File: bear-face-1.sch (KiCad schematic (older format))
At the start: 177 parts, among them J1 Conn_01x04, SW1 SW_Push, U1 Elite-C

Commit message: Diodes, silkscreen updated
Changed diodes back to THT diodes to avoid track issues. Intend to use 1N4148 diodes
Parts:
- added H8: Hole, MountingHole:MountingHole_2.1mm, symbol keebio:Hole
- D1, D10, D11, D12, D13, D14, D15, D16, D17, D18, D19, D2, D20, D21, D22, D23, D24, D25, D26, D27, D28, D29, D3, D30, D31, D32, D33, D34, D35, D36, D37, D38, D39, D4, D40, D41, D42, D43, D44, D45, D46, D47, D48, D49, D5, D50, D51, D52, D53, D54, D55, D56, D57, D58, D59, D6, D60, D61, D62, D63, D64, D65, D66, D67, D68, D69, D7, D70, D71, D72, D73, D74, D75, D76, D77, D78, D79, D8, D80, D81, D82, D83, D9: footprint Keebio-Parts:Diode-dual -> Keebio-Parts:Diode

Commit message: Added hole for plate ground
Stock plate has a hole grounding the plate to the PCB. Added this hole as a 3mm mounting hole (H8)
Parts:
- H8: footprint MountingHole:MountingHole_2.1mm -> MountingHole:MountingHole_3mm
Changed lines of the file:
@@
 F 0 "H8" H 3186 2053 60  0000 L CNN
 F 1 "Hole" H 3186 1947 60  0000 L CNN
-F 2 "MountingHole:MountingHole_2.1mm" H 3000 2000 60  0001 C CNN
+F 2 "MountingHole:MountingHole_3mm" H 3000 2000 60  0001 C CNN
 F 3 "" H 3000 2000 60  0001 C CNN
 	1    3000 2000

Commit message: Matrix, footprints changed
Changed to pure rectangular matrix, updated switch and diode SilkS, anticipate using on-board 32u4
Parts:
- removed J1: Conn_01x04, Connector_Wire:SolderWirePad_1x04_P3.175mm_Drill0.8mm, symbol Connector_Generic:Conn_01x04
- removed U1: Elite-C, Keebio-Parts:Elite-C, symbol keebio:Elite-C
- added F1: 500mA, Fuse:Fuse_1206_3216Metric, symbol Device:Polyfuse_Small
- renumbered D11 to D1, D16 to D10, D17 to D11, D7 to D12, D8 to D13, D18 to D14, D10 to D15, D21 to D16, D22 to D17, D12 to D18, D23 to D19, D1 to D2, D14 to D20, D24 to D21, D33 to D22, D34 to D23, D25 to D24, D35 to D25, D36 to D28, D28 to D29, D2 to D3, D20 to D30, D30 to D31, D31 to D32, D40 to D33, D32 to D34, D41 to D35, D51 to D36, D42 to D37, D43 to D38, D52 to D39, D13 to D4, D44 to D40, D53 to D41, D45 to D42, D46 to D43, D37 to D44, D9 to D45, D39 to D46, D58 to D47, D49 to D48, D59 to D49, D3 to D5, D60 to D51, D70 to D52, D61 to D53, D71 to D54, D62 to D55, D63 to D56, D54 to D57, D55 to D58, D19 to D59, D4 to D6, D48 to D60, D67 to D61, D76 to D62, D68 to D63, D77 to D64, D69 to D65, D79 to D66, D80 to D67, D81 to D68, D72 to D69, D5 to D7, D73 to D70, D64 to D71, D29 to D72, D38 to D73, D57 to D74, D66 to D75, D75 to D76, D78 to D77, D82 to D78, D83 to D79, D15 to D8, D74 to D80, D65 to D81, D56 to D82, D47 to D83, D6 to D9, H3 to H2, H5 to H3, H7 to H4, H2 to H5, H4 to H6, H6 to H7, MX11 to MX1, MX16 to MX10, MX17 to MX11, MX7 to MX12, MX8 to MX13, MX18 to MX14, MX10 to MX15, MX21 to MX16, MX22 to MX17, MX12 to MX18, MX23 to MX19, MX1 to MX2, MX14 to MX20, MX24 to MX21, MX33 to MX22, MX34 to MX23, MX25 to MX24, MX35 to MX25, MX36 to MX28, MX28 to MX29, MX2 to MX3, MX20 to MX30, MX30 to MX31, MX31 to MX32, MX40 to MX33, MX32 to MX34, MX41 to MX35, MX51 to MX36, MX42 to MX37, MX43 to MX38, MX52 to MX39, MX13 to MX4, MX44 to MX40, MX53 to MX41, MX45 to MX42, MX46 to MX43, MX37 to MX44, MX9 to MX45, MX39 to MX46, MX58 to MX47, MX49 to MX48, MX59 to MX49, MX3 to MX5, MX60 to MX51, MX70 to MX52, MX61 to MX53, MX71 to MX54, MX62 to MX55, MX63 to MX56, MX54 to MX57, MX55 to MX58, MX19 to MX59, MX4 to MX6, MX48 to MX60, MX67 to MX61, MX76 to MX62, MX68 to MX63, MX77 to MX64, MX69 to MX65, MX79 to MX66, MX80 to MX67, MX81 to MX68, MX72 to MX69, MX5 to MX7, MX73 to MX70, MX64 to MX71, MX29 to MX72, MX38 to MX73, MX57 to MX74, MX66 to MX75, MX75 to MX76, MX78 to MX77, MX82 to MX78, MX83 to MX79, MX15 to MX8, MX74 to MX80, MX65 to MX81, MX56 to MX82, MX47 to MX83, MX6 to MX9
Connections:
- net labels added: COL10, COL11, COL12, COL13, COL14
- net labels removed: ROW6, ROW7, ROW8
- wire segments 260 -> 254
- no-connect marks 5 -> 0
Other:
- moved on the sheet: D1, D10, D11, D12, D13, D14, D15, D16, D17, D18, D19, D2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

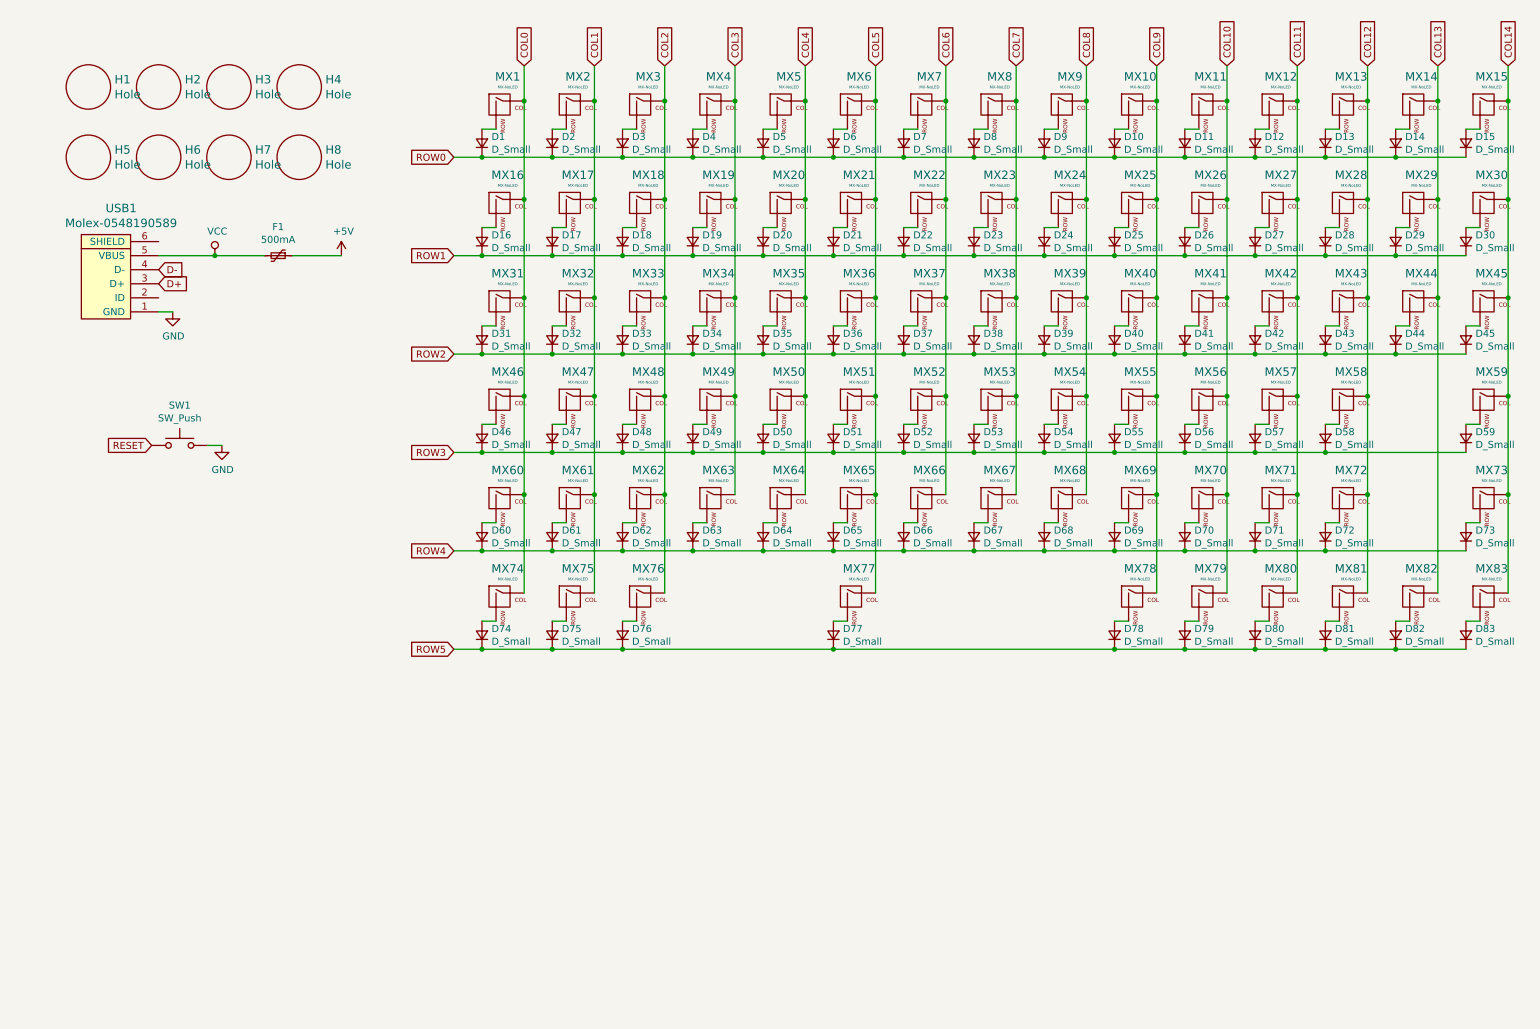
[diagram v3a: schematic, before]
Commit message: MCU added, diodes changed
Changed to SMD components, matched components used in ai03's guide
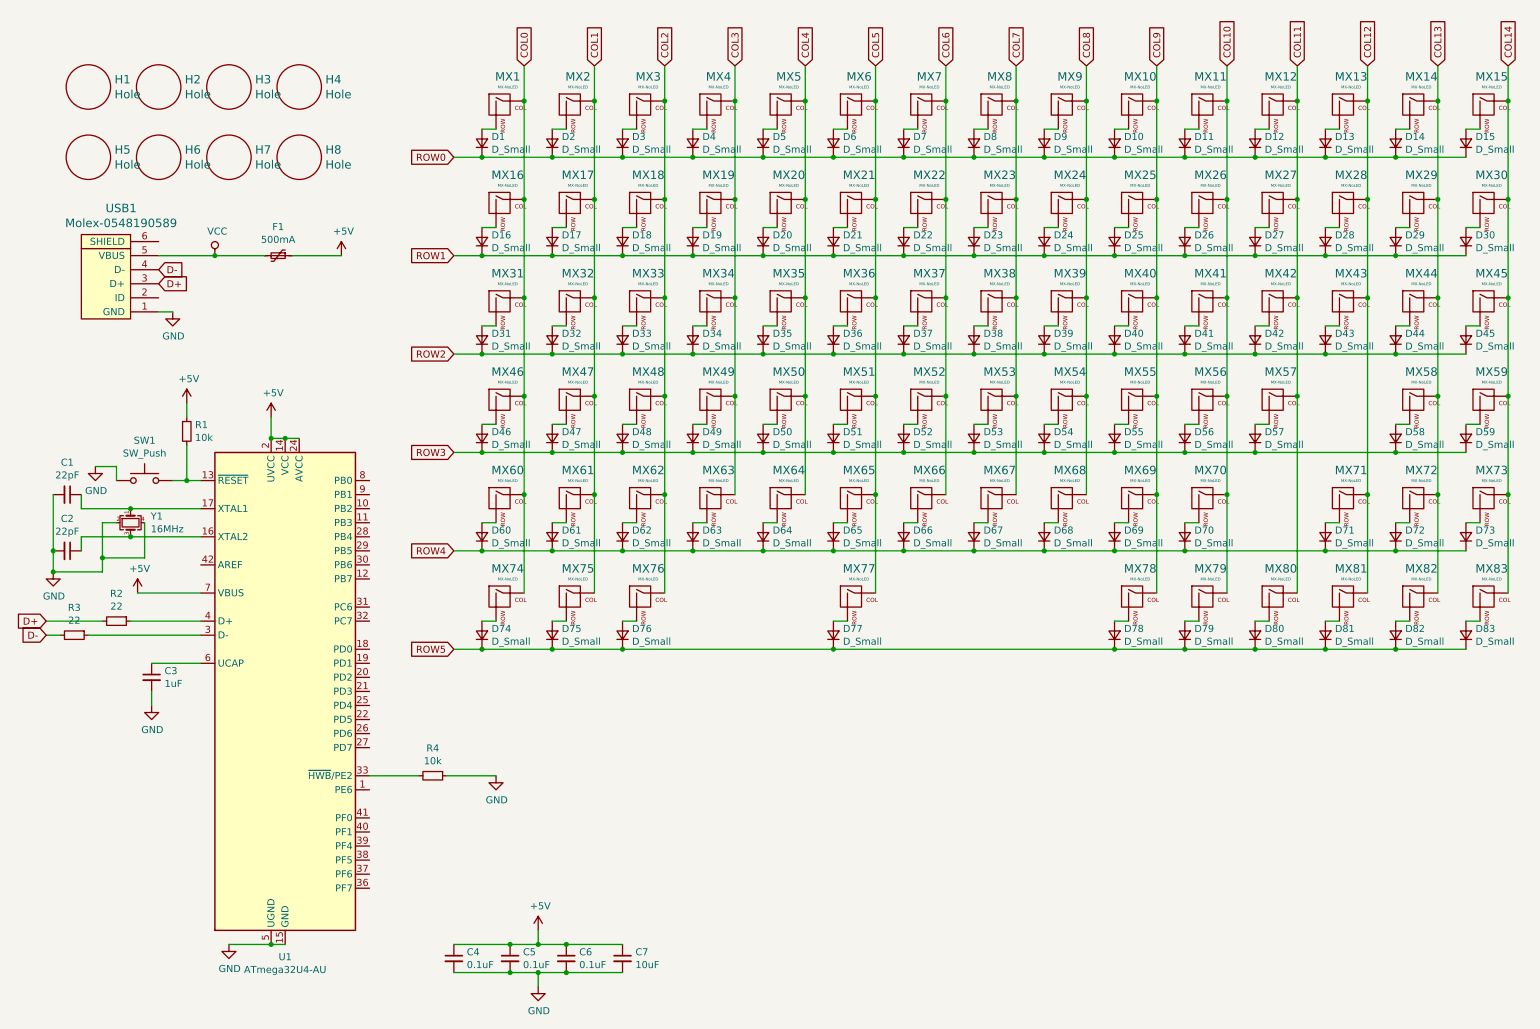
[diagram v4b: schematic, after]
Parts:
- added C1, C2: 22pF, Capacitor_SMD:C_0805_2012Metric, symbol Device:C_Small
- added C3: 1uF, Capacitor_SMD:C_0805_2012Metric, symbol Device:C_Small
- added C4, C5, C6: 0.1uF, Capacitor_SMD:C_0805_2012Metric, symbol Device:C_Small
- added C7: 10uF, Capacitor_SMD:C_0805_2012Metric, symbol Device:C_Small
- added R1, R4: 10k, Resistor_SMD:R_0805_2012Metric, symbol Device:R_Small
- added R2, R3: 22, Resistor_SMD:R_0805_2012Metric, symbol Device:R_Small
- added U1: ATmega32U4-AU, Package_QFP:TQFP-44_10x10mm_P0.8mm, symbol MCU_Microchip_ATmega:ATmega32U4-AU
- added Y1: 16MHz, Crystal:Crystal_SMD_3225-4Pin_3.2x2.5mm, symbol Device:Crystal_GND24_Small
- D1, D10, D11, D12, D13, D14, D15, D16, D17, D18, D19, D2, D20, D21, D22, D23, D24, D25, D26, D27, D28, D29, D3, D30, D31, D32, D33, D34, D35, D36, D37, D38, D39, D4, D40, D41, D42, D43, D44, D45, D46, D47, D48, D49, D5, D50, D51, D52, D53, D54, D55, D56, D57, D58, D59, D6, D60, D61, D62, D63, D64, D65, D66, D67, D68, D69, D7, D70, D71, D72, D73, D74, D75, D76, D77, D78, D79, D8, D80, D81, D82, D83, D9: footprint Keebio-Parts:Diode -> Diode_SMD:D_SOD-123
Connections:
- net RESET is gone; now on net GND: SW1.1
- net +5V: now also C4.1, C5.1, C6.1, C7.1, R1.1, U1.14 (VCC), U1.2 (UVCC), U1.24 (AVCC), U1.34 (VCC), U1.44 (AVCC), U1.7 (VBUS)
- net COL11: no longer MX71.1 (COL)
- net COL12: now also MX71.1 (COL); no longer MX58.1 (COL), MX72.1 (COL)
- net COL13: now also MX58.1 (COL), MX72.1 (COL)
- net D+: now also R2.2
- net D-: now also R3.2
- net GND: now also C1.2, C2.2, C3.2, C4.2, C5.2, C6.2, C7.2, R4.1, U1.15 (GND), U1.23 (GND), U1.35 (GND), U1.43 (GND), U1.5 (UGND), Y1.2, Y1.4; no longer SW1.2
- new net: R1.2, SW1.2, U1.13 (~RESET)
- new net: C2.1, U1.16 (XTAL2), Y1.3
- new net: C1.1, U1.17 (XTAL1), Y1.1
- new net: R3.1, U1.3 (D-)
- new net: R4.2, U1.33 (~HWB~/PE2)
- new net: R2.1, U1.4 (D+)
- new net: C3.1, U1.6 (UCAP)
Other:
- moved on the sheet: D58, D71, D72, MX58, MX71, MX72, SW1

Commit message: Diode footprints updated, MCU components started
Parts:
- D1, D10, D11, D12, D13, D14, D15, D16, D17, D18, D19, D2, D20, D21, D22, D23, D24, D25, D26, D27, D28, D29, D3, D30, D31, D32, D33, D34, D35, D36, D37, D38, D39, D4, D40, D41, D42, D43, D44, D45, D46, D47, D48, D49, D5, D50, D51, D52, D53, D54, D55, D56, D57, D58, D59, D6, D60, D61, D62, D63, D64, D65, D66, D67, D68, D69, D7, D70, D71, D72, D73, D74, D75, D76, D77, D78, D79, D8, D80, D81, D82, D83, D9: footprint Diode_SMD:D_SOD-123 -> Bear-Face-1_parts:D_SOD-123
- MX77: footprint MX_Only:MXOnly-6.25U-NoLED -> MX_Only:MXOnly-6.25U-ReversedStabilizers-NoLED

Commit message: Short diode tracks added
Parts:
- SW1: footprint random-keyboard-parts:PushButton_6x6mm_TH_Pretty -> random-keyboard-parts:SKQG-1155865
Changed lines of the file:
@@
 F 0 "SW1" H 1400 4085 50  0000 C CNN
 F 1 "SW_Push" H 1400 3994 50  0000 C CNN
-F 2 "random-keyboard-parts:PushButton_6x6mm_TH_Pretty" H 1400 4000 50  0001 C CNN
+F 2 "random-keyboard-parts:SKQG-1155865" H 1400 4000 50  0001 C CNN
 F 3 "~" H 1400 4000 50  0001 C CNN
 	1    1400 3800

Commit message: THT diodes and short tracks
Changed to use a combination of THT and SMD components
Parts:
- D1, D10, D11, D12, D13, D14, D15, D16, D17, D18, D19, D2, D20, D21, D22, D23, D24, D25, D26, D27, D28, D29, D3, D30, D31, D32, D33, D34, D35, D36, D37, D38, D39, D4, D40, D41, D42, D43, D44, D45, D46, D47, D48, D49, D5, D50, D51, D52, D53, D54, D55, D56, D57, D58, D59, D6, D60, D61, D62, D63, D64, D65, D66, D67, D68, D69, D7, D70, D71, D72, D73, D74, D75, D76, D77, D78, D79, D8, D80, D81, D82, D83, D9: footprint Bear-Face-1_parts:D_SOD-123 -> Keebio-Parts:Diode
- SW1: footprint random-keyboard-parts:SKQG-1155865 -> random-keyboard-parts:PushButton_6x6mm_TH_Pretty
- U1: footprint Package_QFP:TQFP-44_10x10mm_P0.8mm -> Keebio-Parts:ATMEGA32U4-AU

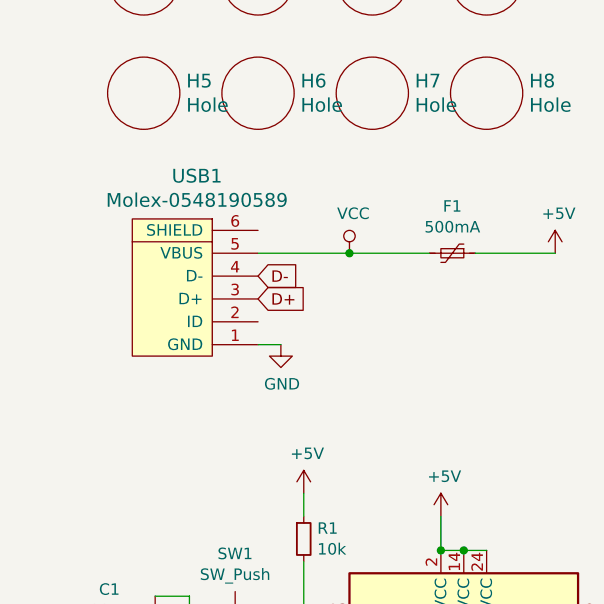
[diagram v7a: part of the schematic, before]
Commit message: Fixed dPair, USB connector schematic
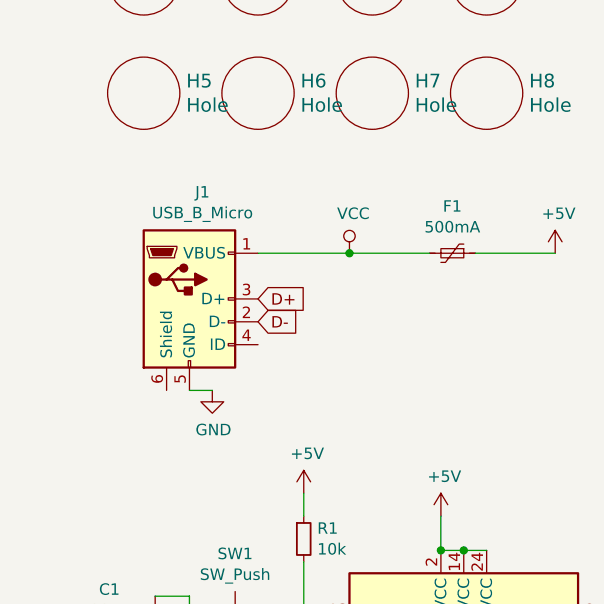
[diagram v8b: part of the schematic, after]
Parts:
- removed USB1: Molex-0548190589, Connector_USB:USB_Micro-B_GCT_USB3076-30-A, symbol random-keyboard-parts:Molex-0548190589
- added J1: USB_B_Micro, Connector_USB:USB_Micro-B_Wuerth_629105150521, symbol Connector:USB_B_Micro
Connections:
- net D+: now also J1.3 (D+)
- net D-: now also J1.2 (D-)
- net GND: now also J1.5 (GND)
- net VCC: now also J1.1 (VBUS)
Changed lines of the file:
@@
 Comment4 ""
 $EndDescr
-$Comp
-L random-keyboard-parts:Molex-0548190589 USB1
-U 1 1 5E0114F2
-P 1200 2400
-F 0 "USB1" V 1737 2367 60  0000 C CNN
-F 1 "Molex-0548190589" V 1631 2367 60  0000 C CNN
-F 2 "Connector_USB:USB_Micro-B_GCT_USB3076-30-A" H 1200 2400 60  0001 C CNN
-F 3 "" H 1200 2400 60  0001 C CNN
-	1    1200 2400
-	0    -1   -1   0
-$EndComp
 Wire Wire Line
 	8800 4800 8900 4800
@@
 	1    0    0    -1
 $EndComp
-Text GLabel 1500 2300 2    50   Input ~ 0
+Text GLabel 1500 2500 2    50   Input ~ 0
 D-
 Text GLabel 1500 2400 2    50   Input ~ 0
@@
 L power:GND #PWR0103
 U 1 1 5E22CB98
-P 1600 2600
-F 0 "#PWR0103" H 1600 2350 50  0001 C CNN
-F 1 "GND" H 1605 2427 50  0000 C CNN
-F 2 "" H 1600 2600 50  0001 C CNN
-F 3 "" H 1600 2600 50  0001 C CNN
-	1    1600 2600
+P 1300 2800
+F 0 "#PWR0103" H 1300 2550 50  0001 C CNN
+F 1 "GND" H 1305 2627 50  0000 C CNN
+F 2 "" H 1300 2800 50  0001 C CNN
+F 3 "" H 1300 2800 50  0001 C CNN
+	1    1300 2800
 	1    0    0    -1
 $EndComp
 Wire Wire Line
-	1600 2600 1500 2600
+	1300 2800 1200 2800
 Wire Wire Line
 	3600 1500 3800 1500
@@
 Wire Wire Line
 	1000 4900 1800 4900
+$Comp
+L Connector:USB_B_Micro J1
+U 1 1 5E3DEFC6
+P 1200 2400
+F 0 "J1" H 1257 2867 50  0000 C CNN
+F 1 "USB_B_Micro" H 1257 2776 50  0000 C CNN
+F 2 "Connector_USB:USB_Micro-B_Wuerth_629105150521" H 1350 2350 50  0001 C CNN
+F 3 "~" H 1350 2350 50  0001 C CNN
+	1    1200 2400
+	1    0    0    -1
+$EndComp
 $EndSCHEMATC
